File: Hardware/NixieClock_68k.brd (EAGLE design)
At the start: 100 x 100 mm, 70 parts, among them IC1 68008, IC10 7805, IC11 MIC803, IC2 AS6C1008, IC3 39SF020, IC4 DS1244Y, IC5 FT245R, IC6 NE555, IC7 ATF1504AS, IC8 74HC377N, IC9 74HC373N, X1 4MHz

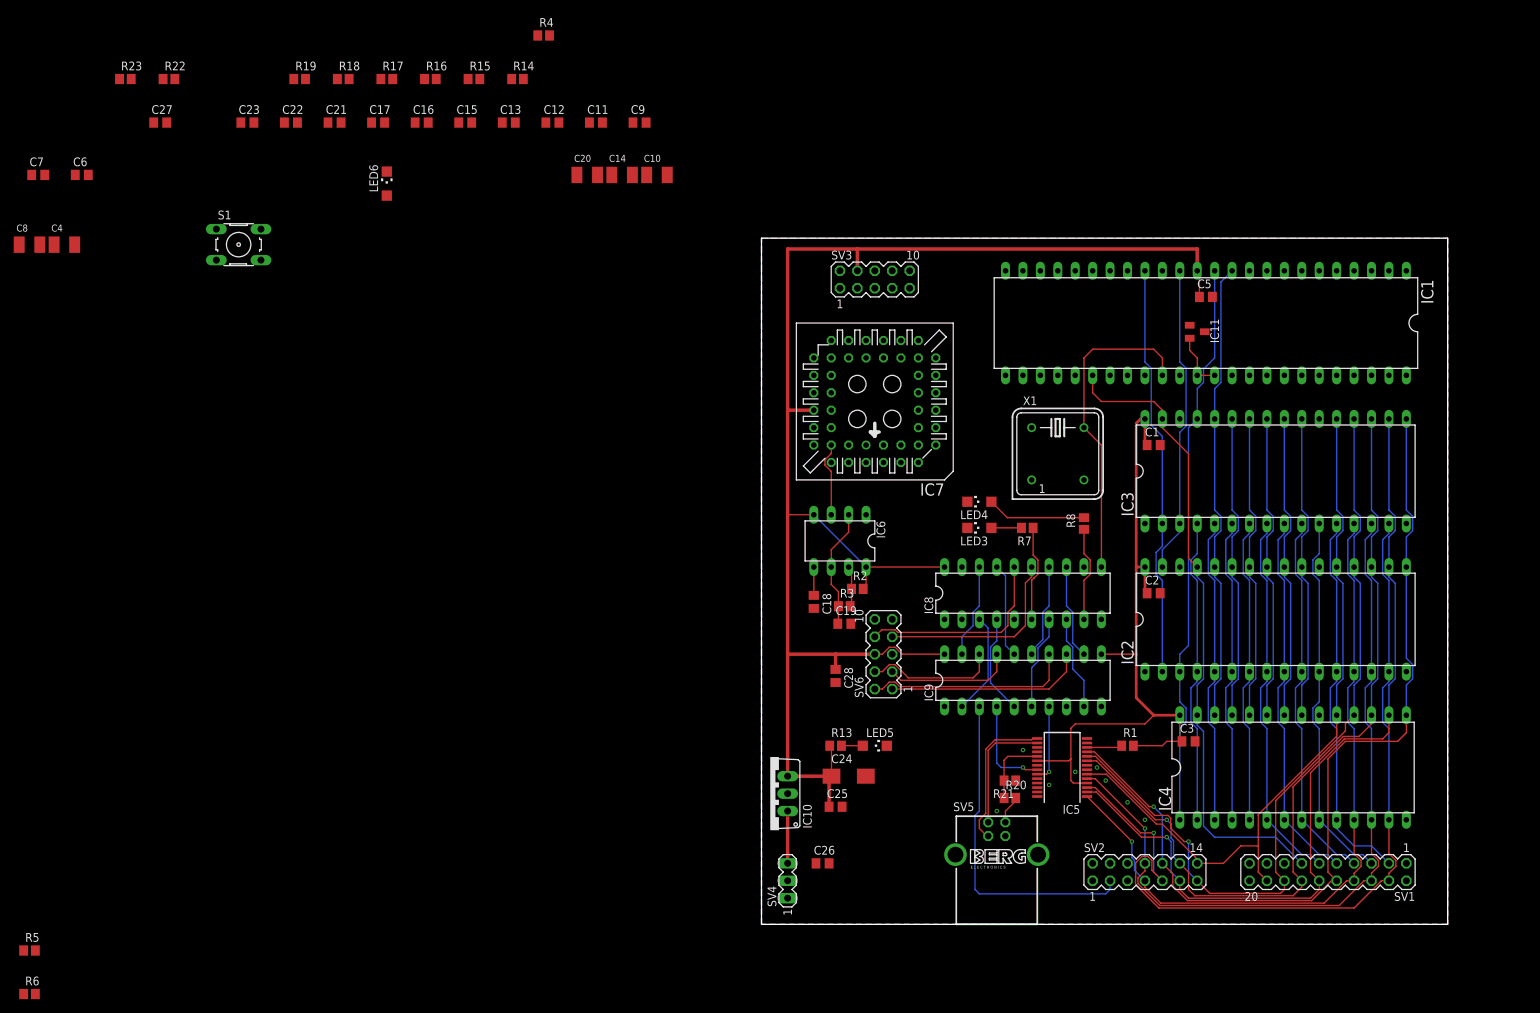
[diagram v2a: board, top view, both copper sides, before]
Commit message: more routing of address bus
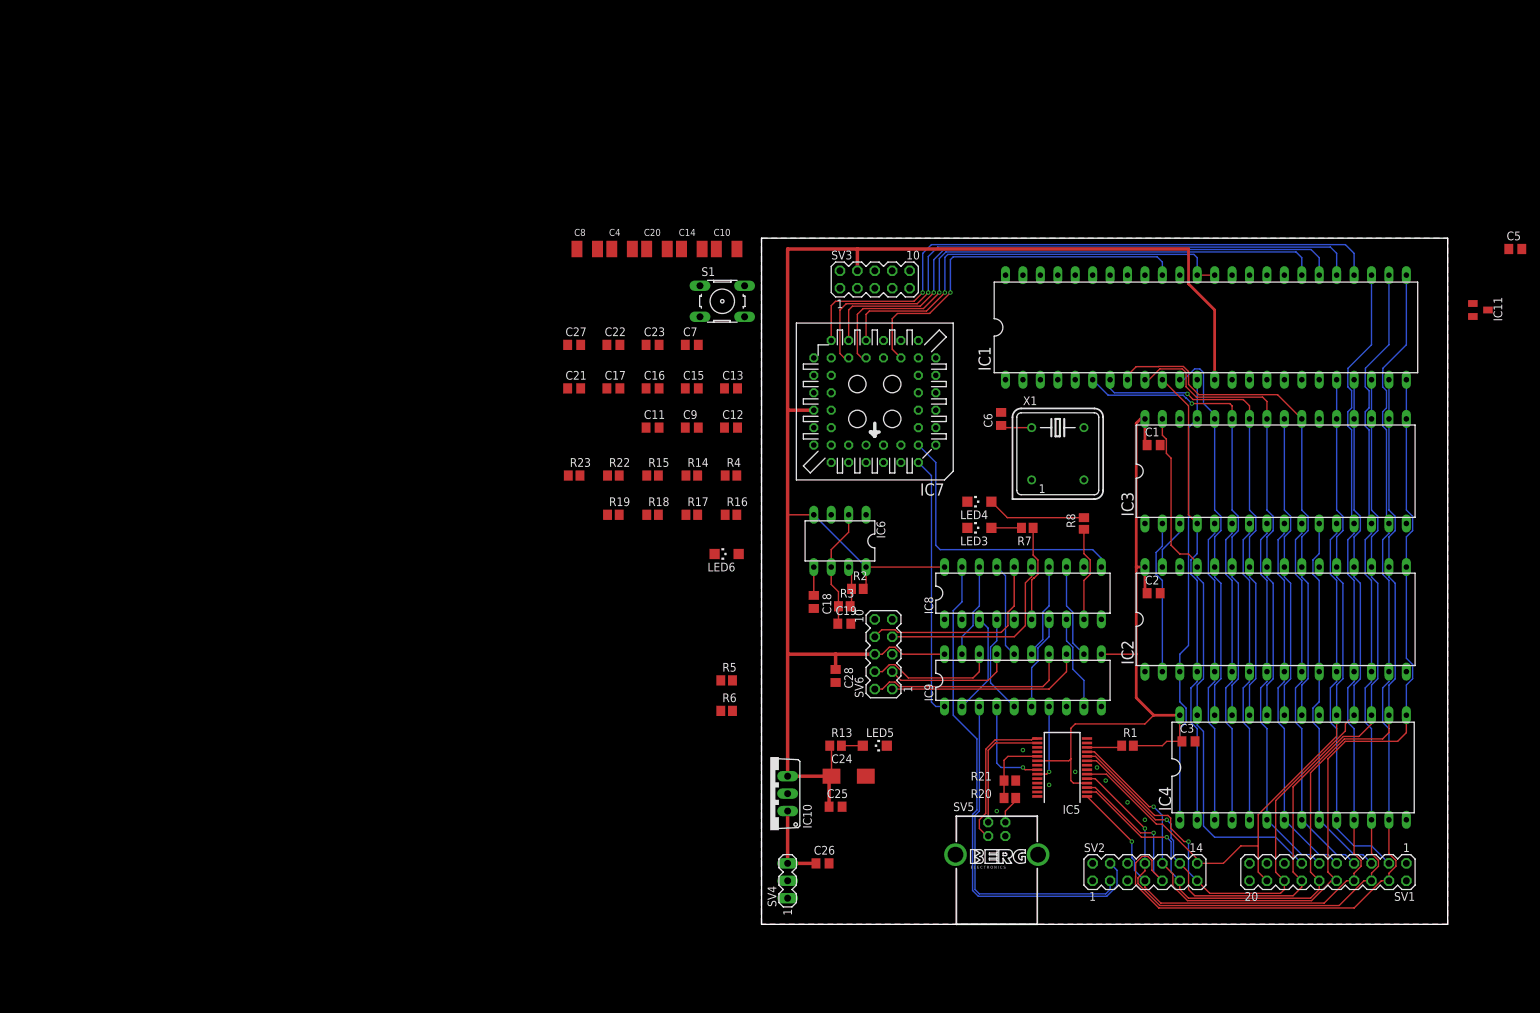
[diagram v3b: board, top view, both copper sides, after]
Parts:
- IC8: value 74HC377N -> 74HC374N
- moved C6 138.6 mm to (34.9, 73.7), turned to 90 degrees
- moved R6 109.7 mm to (-5.08, 31.1)
- moved R5 109.0 mm to (-5.08, 35.6)
- moved C7 98.4 mm to (-10.2, 84.5)
- moved R23 87.3 mm to (-27.3, 65.4)
- moved R22 86.8 mm to (-21.6, 65.4)
- moved C4 81.3 mm to (-20.3, 98.4)
- moved C8 81.3 mm to (-25.4, 98.4)
- moved R19 78.2 mm to (-21.6, 59.7)
- moved R18 77.9 mm to (-15.9, 59.7)
- moved R17 77.5 mm to (-10.2, 59.7)
- moved R16 77.1 mm to (-4.45, 59.7)
- moved LED6 73.3 mm to (-5.08, 54.0), turned to 90 degrees
- moved S1 71.0 mm to (-5.71, 90.8)
- moved R4 69.7 mm to (-4.45, 65.4)
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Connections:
- new net N$11: IC7.14
- new net N$12: IC7.18
- new net N$13: IC7.19
- new net N$14: IC7.20
- new net N$21: IC7.29
- new net N$22: IC7.31
- new net N$23: IC7.33
- new net N$24: IC7.34
- new net N$25: IC7.36
- new net N$26: IC7.37
- new net N$27: IC7.39
- new net N$28: IC7.40
- new net N$29: IC7.1
- new net N$3: IC7.17
- new net N$30: IC7.44
- new net N$31: IC7.41
- new net N$32: IC7.4
- new net N$33: IC7.5
- new net N$36: IC7.9
- new net N$37: IC7.11
- new net N$38: IC7.12
- new net N$5: IC7.16
- net !AS: now also IC7.28; no longer IC7.1, SV1.15
- net !DS: now also IC7.27; no longer IC7.44
- net !DTACK: now also IC7.25; no longer IC7.20
- net !IO_IN_CS: now also IC7.6; no longer IC7.24
- net !IO_OUT_CS: now also IC7.8, IC8.11; no longer IC7.25, IC8.1
- net !IPL0/2: no longer IC7.14
- net !IPL1: no longer IC7.12
- net !NIXIE_CS: no longer IC7.31
- net !OE: no longer IC7.39
- net !RAM_CS: no longer IC7.36
- net !RESET: now also IC7.24; no longer IC7.21
- net !ROM_CS: no longer IC7.37
- net !RTC_CS: no longer IC7.34
- net !USB_RD: no longer IC7.28
- net !USB_RXF: no longer IC7.26
- net !USB_TXE: no longer IC7.27
- net !VFD_WR: no longer IC7.33
- net !VPA: now also IC7.21; no longer IC7.16
- net A15: no longer IC7.4
- net A16: no longer IC7.5
- net A17: no longer IC7.6
- net A18: no longer IC7.8
- net A19: no longer IC7.9
- net CLK: no longer IC8.11
- net FC0: no longer IC7.17
- net FC1: no longer IC7.18
- net FC2: no longer IC7.19
- net GND: now also IC8.1
- net R/!W!: now also IC7.26; no longer IC7.11
- net TIMER_IRQ: no longer IC7.41
- net USB_WR: no longer IC7.29
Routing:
- net !AS: track 0.00 -> 92.0 mm, vias 0 -> 1
- net !DS: track 0.00 -> 90.7 mm, vias 0 -> 1
- net !DTACK: track 0.00 -> 81.6 mm, vias 0 -> 1
- net !VFD_RESET: track 0.00 -> 75.1 mm
- net R/!W!: track 94.2 -> 163.7 mm, vias 0 -> 1
- net !RESET: track 8.40 -> 64.0 mm, vias 0 -> 1
- net !VPA: track 0.00 -> 54.4 mm, vias 0 -> 1
- net CLK: track 46.6 -> 0.00 mm
- net !IO_OUT_CS: track 0.00 -> 41.8 mm
- net D0: track 118.7 -> 157.2 mm
- net D2: track 137.9 -> 176.4 mm
- net D1: track 125.7 -> 164.2 mm
- net !IO_IN_CS: track 0.00 -> 37.9 mm
- net A16: track 60.2 -> 22.3 mm
- net A15: track 45.0 -> 7.40 mm
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
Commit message: cleaned up routing of busses for memories
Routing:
- net A0: track 55.7 -> 133.6 mm
- net A1: track 54.9 -> 131.3 mm
- net A2: track 54.9 -> 131.3 mm
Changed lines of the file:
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@@
 <contactref element="R5" pad="2"/>
 <contactref element="IC8" pad="1"/>
+<via x="78.74" y="90.17" extent="1-16" drill="0.35"/>
+<via x="78.74" y="76.835" extent="1-16" drill="0.35"/>
+<via x="80.01" y="55.245" extent="1-16" drill="0.35"/>
+<via x="80.01" y="33.655" extent="1-16" drill="0.35"/>
+<via x="80.01" y="26.035" extent="1-16" drill="0.35"/>
+<via x="77.47" y="26.035" extent="1-16" drill="0.35"/>
+<via x="74.93" y="26.035" extent="1-16" drill="0.35"/>
+<via x="72.39" y="26.035" extent="1-16" drill="0.35"/>
+<via x="69.85" y="26.035" extent="1-16" drill="0.35"/>
+<via x="67.31" y="26.035" extent="1-16" drill="0.35"/>
+<via x="62.23" y="24.765" extent="1-16" drill="0.35"/>
+<via x="82.55" y="49.53" extent="1-16" drill="0.35"/>
+<via x="82.55" y="39.37" extent="1-16" drill="0.35"/>
+<via x="81.28" y="71.12" extent="1-16" drill="0.35"/>
+<via x="81.28" y="62.23" extent="1-16" drill="0.35"/>
+<via x="81.28" y="90.17" extent="1-16" drill="0.35"/>
 <wire x1="103.675" y1="90.485" x2="110.805" y2="98.425" width="0" layer="19" extent="1-1"/>
-<wire x1="93.98" y1="58.42" x2="103.675" y2="90.485" width="0" layer="19" extent="1-1"/>
+<wire x1="81.28" y1="90.17" x2="103.675" y2="90.485" width="0" layer="19" extent="1-1"/>
 <wire x1="-2.4638" y1="88.5444" x2="10.16" y2="82.55" width="0" layer="19" extent="1-1"/>
 <wire x1="-8.9662" y1="88.5444" x2="-2.4638" y2="88.5444" width="0" layer="19" extent="1-1"/>
@@
 <wire x1="86.36" y1="11.43" x2="88.9" y2="11.43" width="0.2032" layer="16"/>
 <wire x1="88.9" y1="11.43" x2="91.44" y2="8.89" width="0.2032" layer="16"/>
-<wire x1="83.82" y1="58.42" x2="40.64" y2="94.615" width="0" layer="19" extent="1-1"/>
+<wire x1="40.64" y1="94.615" x2="40.64" y2="92.71" width="0.2032" layer="16"/>
+<wire x1="40.64" y1="92.71" x2="41.275" y2="92.075" width="0.2032" layer="16"/>
+<wire x1="41.275" y1="92.075" x2="81.915" y2="92.075" width="0.2032" layer="16"/>
+<wire x1="81.915" y1="92.075" x2="82.55" y2="91.44" width="0.2032" layer="16"/>
+<wire x1="82.55" y1="91.44" x2="82.55" y2="59.69" width="0.2032" layer="16"/>
+<wire x1="82.55" y1="59.69" x2="83.82" y2="58.42" width="0.2032" layer="16"/>
 </signal>
 <signal name="A1">
@@
 <wire x1="86.36" y1="10.16" x2="87.63" y2="10.16" width="0.2032" layer="16"/>
 <wire x1="87.63" y1="10.16" x2="88.9" y2="8.89" width="0.2032" layer="16"/>
-<wire x1="81.28" y1="58.42" x2="38.1" y2="94.615" width="0" layer="19" extent="1-1"/>
+<wire x1="38.1" y1="94.615" x2="40.9956" y2="91.7194" width="0.2032" layer="16"/>
+<wire x1="80.01" y1="90.805" x2="80.01" y2="61.595" width="0.2032" layer="16"/>
+<wire x1="80.01" y1="61.595" x2="81.28" y2="60.325" width="0.2032" layer="16"/>
+<wire x1="81.28" y1="60.325" x2="81.28" y2="58.42" width="0.2032" layer="16"/>
+<wire x1="40.9956" y1="91.7194" x2="79.0956" y2="91.7194" width="0.2032" layer="16"/>
+<wire x1="79.0956" y1="91.7194" x2="80.01" y2="90.805" width="0.2032" layer="16"/>
 </signal>
 <signal name="A2">
@@
 <wire x1="83.82" y1="10.16" x2="85.09" y2="10.16" width="0.2032" layer="16"/>
 <wire x1="85.09" y1="10.16" x2="86.36" y2="8.89" width="0.2032" layer="16"/>
-<wire x1="78.74" y1="58.42" x2="35.56" y2="94.615" width="0" layer="19" extent="1-1"/>
+<wire x1="35.56" y1="94.615" x2="38.8112" y2="91.3638" width="0.2032" layer="16"/>
+<wire x1="76.9112" y1="91.3638" x2="77.47" y2="90.805" width="0.2032" layer="16"/>
+<wire x1="77.47" y1="90.805" x2="77.47" y2="60.325" width="0.2032" layer="16"/>
+<wire x1="77.47" y1="60.325" x2="78.74" y2="59.055" width="0.2032" layer="16"/>
+<wire x1="78.74" y1="59.055" x2="78.74" y2="58.42" width="0.2032" layer="16"/>
+<wire x1="38.8112" y1="91.3638" x2="76.9112" y2="91.3638" width="0.2032" layer="16"/>
 </signal>
 <signal name="A3">
